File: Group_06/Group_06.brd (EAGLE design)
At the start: 72.4 x 63.5 mm, 29 parts, among them J1 POWER_JACKPTH_LOCK, U2 +12v

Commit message: MUX 1
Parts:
- moved J8 17.8 mm to (6.35, 59.7), turned to 0 degrees
- moved U$3 4.02 mm to (15.5, 51.4), turned to 270 degrees
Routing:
- net 5V: track 124.4 -> 228.5 mm, vias 10 -> 13
- net N$14: track 0.00 -> 23.4 mm, vias 0 -> 2
- net MUX_OUT: track 0.00 -> 21.6 mm, vias 0 -> 2
- net N$17: track 0.00 -> 16.9 mm, vias 0 -> 2
- net N$16: track 0.00 -> 16.1 mm, vias 0 -> 2
- net N$15: track 0.00 -> 15.7 mm, vias 0 -> 2
- net N$10: track 0.00 -> 14.9 mm
- net MUX_A0: track 0.00 -> 14.6 mm, vias 0 -> 2
- net N$11: track 0.00 -> 12.8 mm
- net N$13: track 0.00 -> 12.3 mm
- net MUX_A1: track 0.00 -> 12.3 mm, vias 0 -> 2
- net N$12: track 0.00 -> 12.0 mm
- net MUX_A2: track 0.00 -> 9.23 mm
- net N$18: track 25.5 -> 32.3 mm
- net N$9: track 25.2 -> 29.1 mm
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
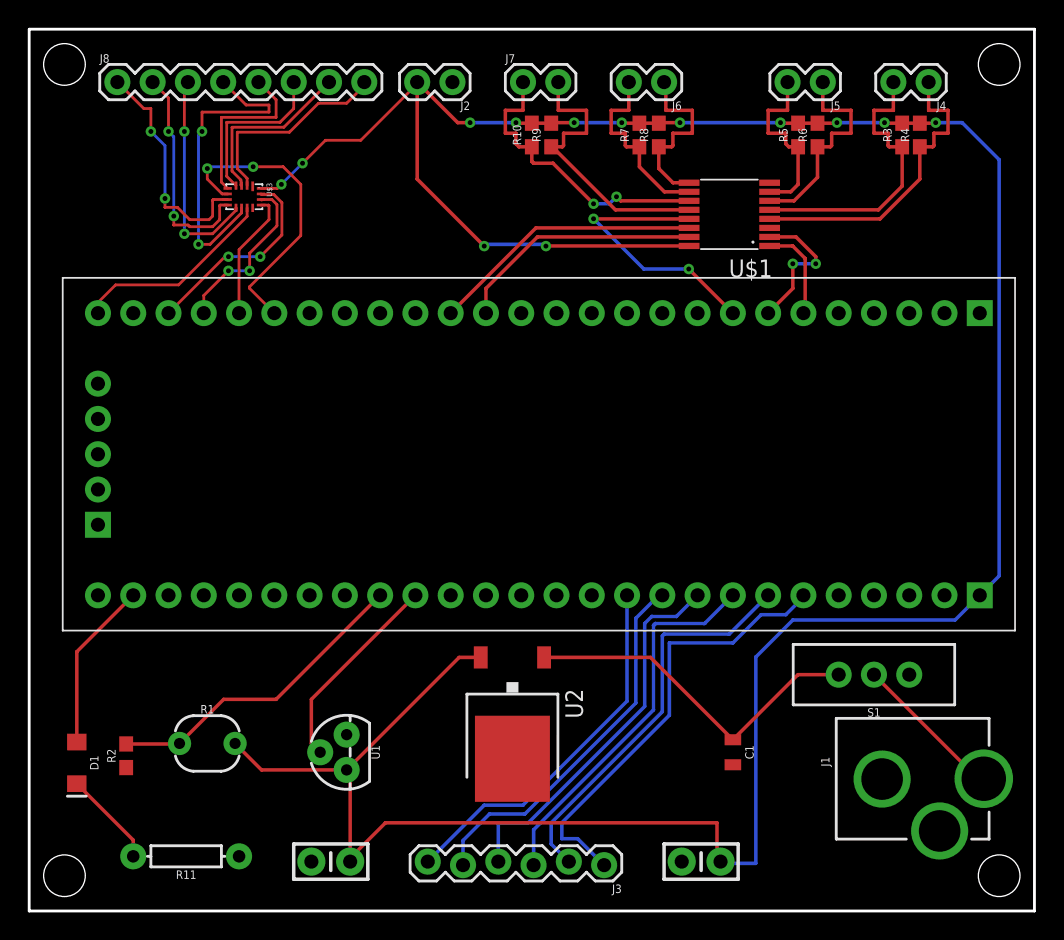
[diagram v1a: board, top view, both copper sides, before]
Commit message: Routing optimization and correct placing tNames
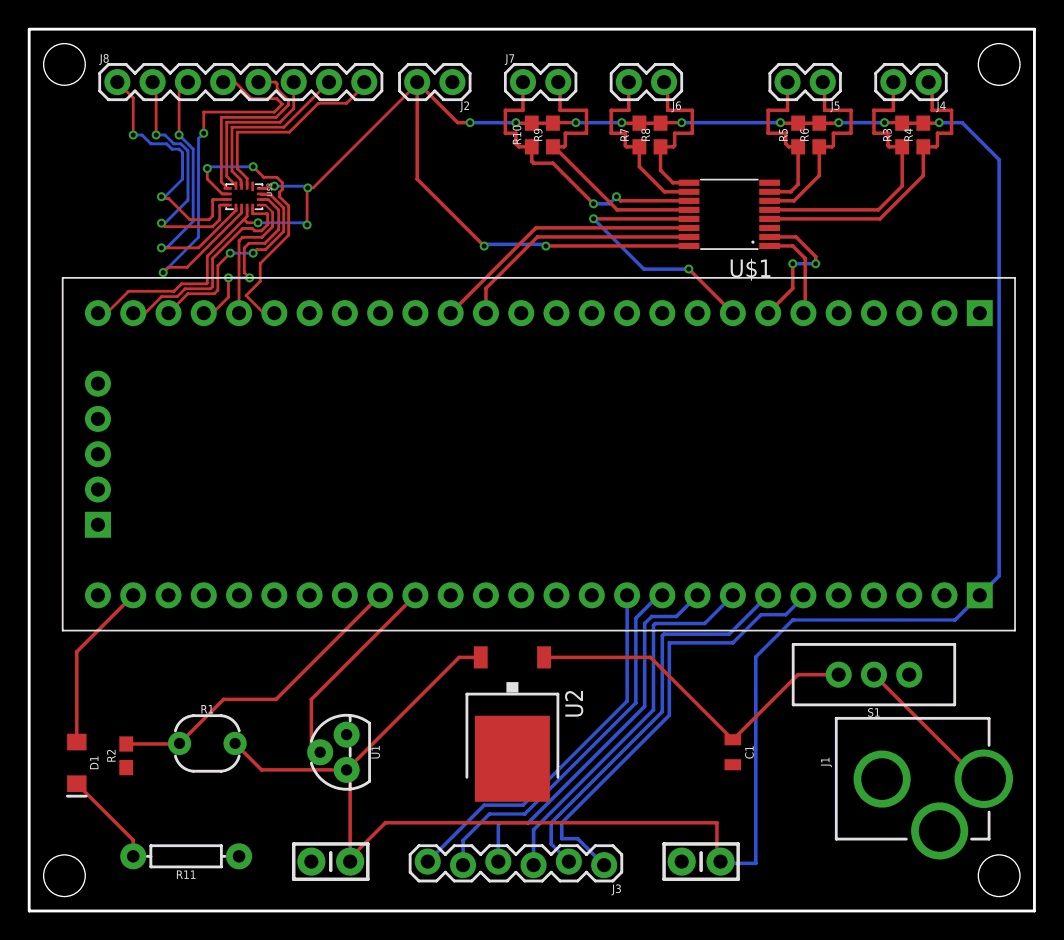
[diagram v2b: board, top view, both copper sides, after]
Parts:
- moved R4 0.25 mm to (64.4, 55.9)
- moved R6 0.13 mm to (56.9, 55.9)
- moved R8 0.13 mm to (45.5, 55.9)
- moved R9 0.13 mm to (37.7, 55.9)
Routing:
- net GND: track 0.00 -> 15.9 mm
- net 5V: track 228.5 -> 236.7 mm, vias 13 -> 15
- net N$14: track 23.4 -> 31.4 mm
- net N$15: track 15.7 -> 20.5 mm
- net N$16: track 16.1 -> 18.9 mm
- net N$17: track 16.9 -> 19.0 mm
- net N$13: track 12.3 -> 13.8 mm
- net MUX_A1: track 12.3 -> 13.5 mm
- net MUX_A0: track 14.6 -> 15.5 mm
- net MUX_A2: track 9.23 -> 10.1 mm
- net MUX_OUT: track 21.6 -> 20.9 mm

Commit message: Silkscreen labels and fixing stop mask interferences
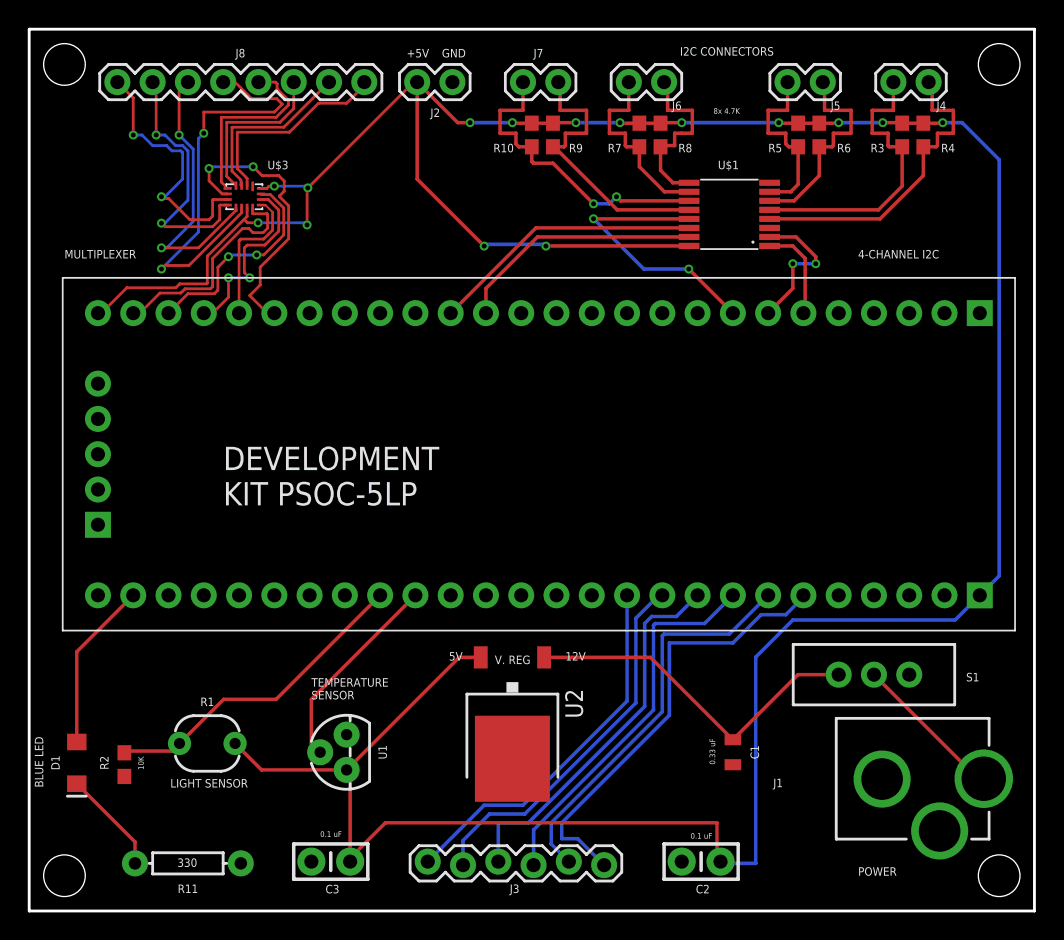
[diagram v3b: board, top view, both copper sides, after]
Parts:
- moved R2 0.65 mm to (6.86, 10.5)
- moved R11 0.52 mm to (11.4, 3.43)
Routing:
- net I2C_SDA_3: track 21.7 -> 22.4 mm
- net N$4: track 6.91 -> 7.47 mm
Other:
- board text added: "+5V"
- board text added: "0.1 uF"
- board text added: "0.33 uF"
- board text added: "10K"
- board text added: "12V"
- board text added: "330"
- board text added: "4-CHANNEL I2C"
- board text added: "5V"
- board text added: "8x 4.7K"
- board text added: "BLUE LED"
- board text added: "C2"
- board text added: "C3"
- board text added: "DEVELOPMENT"
- board text added: "GND"
- board text added: "I2C CONNECTORS"
- board text added: "KIT PSOC-5LP"
- board text added: "LIGHT SENSOR"
- board text added: "MULTIPLEXER"
- board text added: "POWER"
- board text added: "TEMPERATURE SENSOR"
- board text added: "V. REG"
